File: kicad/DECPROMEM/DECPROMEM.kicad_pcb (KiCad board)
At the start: 2 copper layers, 127 x 134.6 mm, 114 parts, among them J10 BDAL08, J11 BDAL09, J12 BDAL10, J13 BDAL11, J14 BDAL12, J15 BDAL13, J16 BDAL14, J17 BDAL15, J18 BDAL16, J19 BDAL17, J2 BDAL00, J20 BDAL18, J21 BDAL19, J22 BDAL20, J23 BDAL21, J24 BRPLYL, J25 BMDENL, J26 BWRITEL, J27 BWLBL, J28 BWHBL, J29 BSDENL, J3 BDAL01, J30 SSnL, J31 BDSL, J32 BASL, J33 BIOSELL, J34 BDCOKH, J35 GND, J36 GND, J37 GND, J38 DAH00, J39 DAH01, J4 BDAL02, J40 DAH02, J41 DAH03, J42 DAH04, J43 DAH05, J44 DAH06, J45 DAH07, J46 DAH08, J47 DAH09, J48 DAH10, J49 DAH11, J5 BDAL03, J50 DAH12, J51 DAH13, J52 DAH14, J53 DAH15, J54 DAH16, J55 DAH17, J56 DAH18, J57 DAH19, J58 DAH20, J59 DAH21, J6 BDAL04, J60 JTAG, J61 ASL, J62 MDENL, J63 SDENL, J64 MOEL, J65 MWEL, J66 MCEHIGHL, J67 MCELOWH, J68 MLEL, J69 MHEL, J7 BDAL05, J70 BUSDIR, J71 BUSOE, J72 CLK, J73 MA15, J74 MA16, J75 MA17, J76 MA18, J77 MA19, J78 MA20, J79 MA21, J8 BDAL06, J80 HOLDL, J81 CSL, J82 SCK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

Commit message: More layout done.
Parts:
- added J85: BINITL, CompLibFootprint:Testpoint, F.Cu at (386.1, 203.8)
- moved J37 112.5 mm to (391.8, 124.5), turned to 0 degrees
- moved R2 88.6 mm to (368.9, 118.1), turned to -90 degrees
- moved C4 60.5 mm to (388.0, 129.5), turned to 90 degrees
- moved J36 54.7 mm to (283.2, 151.1), turned to 0 degrees
- moved C9 36.2 mm to (273.7, 170.2)
- moved C10 31.5 mm to (286.4, 137.2), turned to -90 degrees
- moved J79 30.3 mm to (362.6, 119.4), turned to 0 degrees
- moved J60 24.2 mm to (278.1, 194.3)
- moved C3 22.7 mm to (275.6, 132.1)
- moved R3 20.4 mm to (271.8, 137.2)
- moved J72 19.8 mm to (272.4, 146.7), turned to 0 degrees
- moved C5 18.1 mm to (364.5, 128.2), turned to 90 degrees
- moved J82 15.9 mm to (270.5, 123.2), turned to 180 degrees
- moved J84 14.9 mm to (285.8, 125.7), turned to 0 degrees
- moved J80 14.0 mm to (272.4, 125.7), turned to 180 degrees
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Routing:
- net GND: track 0.00 -> 678.4 mm, vias 0 -> 13
- net +5V: track 0.00 -> 548.8 mm, vias 0 -> 13
- net /BDCOKH: track 0.00 -> 186.3 mm, vias 0 -> 2
- net /BINITL: track 0.00 -> 182.3 mm, vias 0 -> 2
- net /BRPLYL: track 18.2 -> 177.0 mm, vias 0 -> 3
- net /MDENL: track 13.0 -> 158.2 mm, vias 0 -> 2
- net /BWHBL: track 18.1 -> 157.3 mm, vias 0 -> 2
- net /SSnL: track 18.2 -> 156.9 mm, vias 0 -> 2
- net /BMDENL: track 18.2 -> 156.2 mm, vias 0 -> 2
- net /BWRITEL: track 18.1 -> 152.2 mm, vias 0 -> 2
- net /BUSDIRH: track 14.9 -> 147.6 mm, vias 0 -> 2
- net /BUSOEL: track 7.26 -> 133.2 mm, vias 0 -> 4
- net /BSDENL: track 18.1 -> 140.6 mm, vias 0 -> 2
- net /BASL: track 17.1 -> 135.2 mm, vias 0 -> 4
- net /BIOSELL: track 18.1 -> 131.5 mm, vias 0 -> 2
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
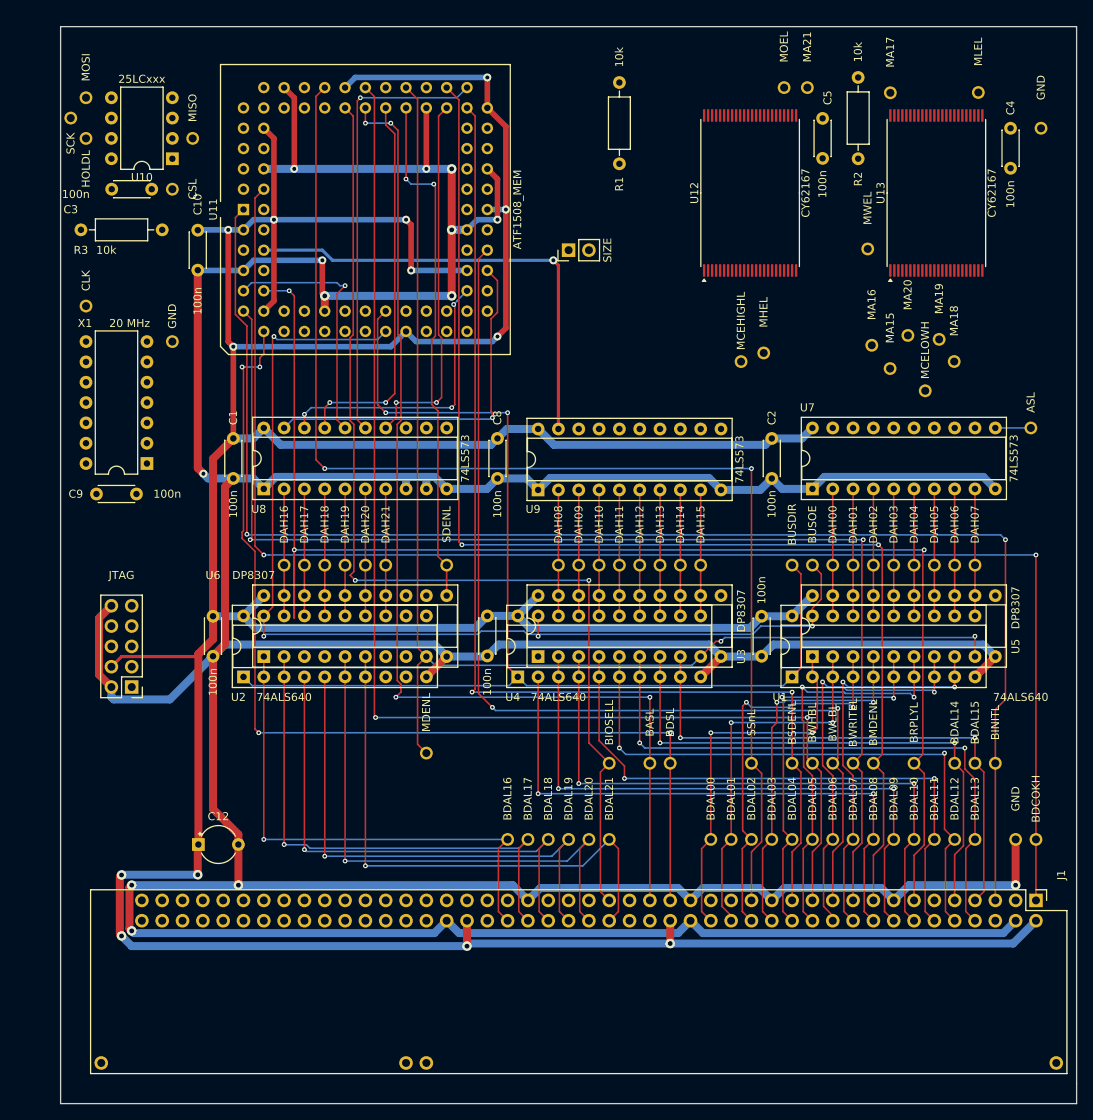
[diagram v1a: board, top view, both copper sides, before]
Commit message: Had to add more test points.
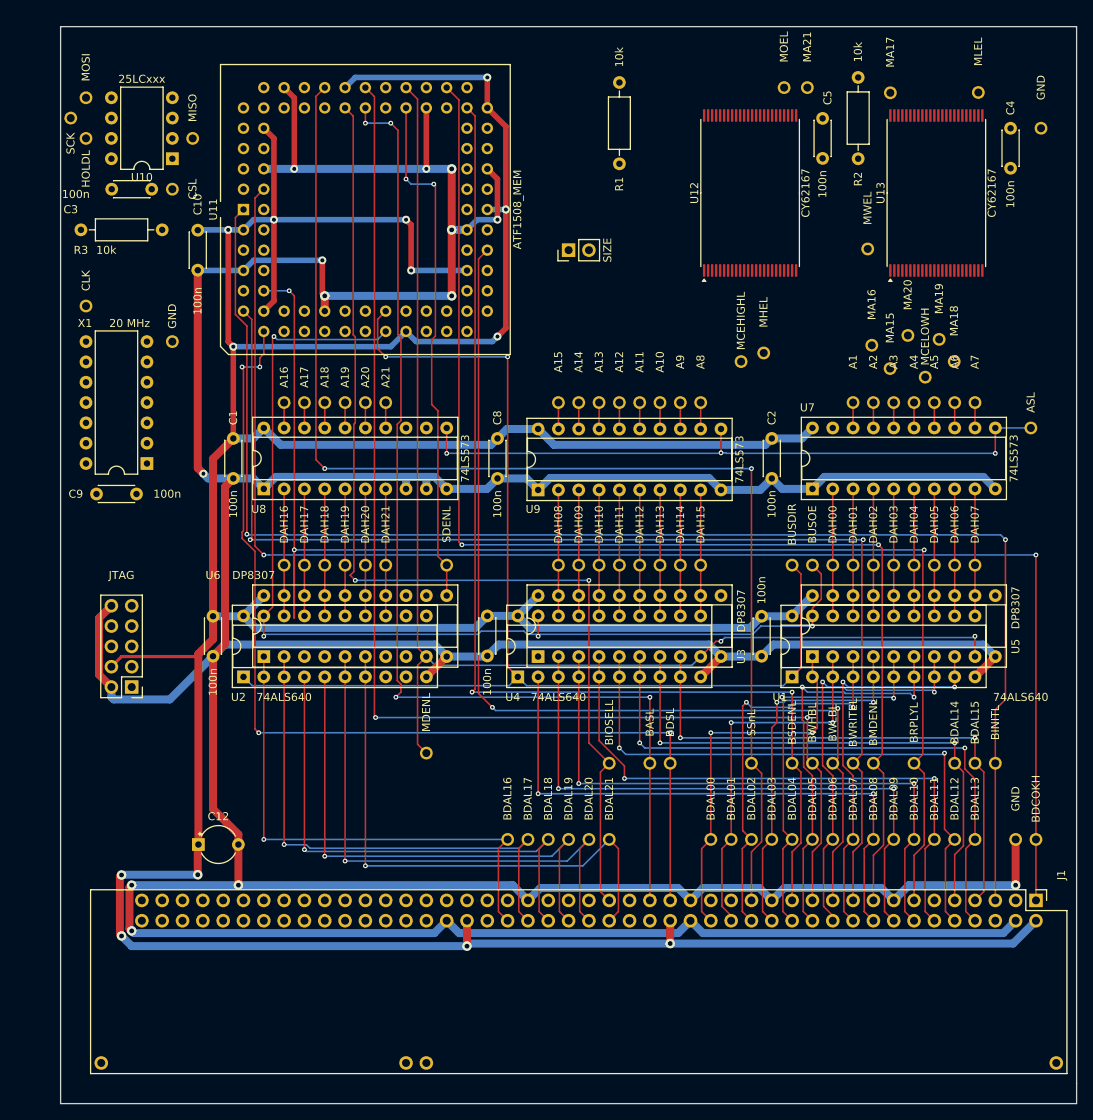
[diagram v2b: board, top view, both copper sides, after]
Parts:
- added J100: A15, CompLibFootprint:Testpoint, F.Cu at (331.5, 158.8)
- added J101: A16, CompLibFootprint:Testpoint, F.Cu at (297.2, 158.8)
- added J102: A17, CompLibFootprint:Testpoint, F.Cu at (299.7, 158.8)
- added J103: A18, CompLibFootprint:Testpoint, F.Cu at (302.3, 158.8)
- added J104: A19, CompLibFootprint:Testpoint, F.Cu at (304.8, 158.8)
- added J105: A20, CompLibFootprint:Testpoint, F.Cu at (307.3, 158.8)
- added J106: A21, CompLibFootprint:Testpoint, F.Cu at (309.9, 158.8)
- added J86: A1, CompLibFootprint:Testpoint, F.Cu at (368.3, 158.8)
- added J87: A2, CompLibFootprint:Testpoint, F.Cu at (370.8, 158.8)
- added J88: A3, CompLibFootprint:Testpoint, F.Cu at (373.4, 158.8)
- added J89: A4, CompLibFootprint:Testpoint, F.Cu at (375.9, 158.8)
- added J90: A5, CompLibFootprint:Testpoint, F.Cu at (378.5, 158.8)
- added J91: A6, CompLibFootprint:Testpoint, F.Cu at (381.0, 158.8)
- added J92: A7, CompLibFootprint:Testpoint, F.Cu at (383.5, 158.8)
- added J93: A8, CompLibFootprint:Testpoint, F.Cu at (349.2, 158.8)
- added J94: A9, CompLibFootprint:Testpoint, F.Cu at (346.7, 158.8)
- added J95: A10, CompLibFootprint:Testpoint, F.Cu at (344.2, 158.8)
- added J96: A11, CompLibFootprint:Testpoint, F.Cu at (341.6, 158.8)
- added J97: A12, CompLibFootprint:Testpoint, F.Cu at (339.1, 158.8)
- added J98: A13, CompLibFootprint:Testpoint, F.Cu at (336.6, 158.8)
- added J99: A14, CompLibFootprint:Testpoint, F.Cu at (334.0, 158.8)
- moved J67 1.71 mm to (377.3, 155.6)
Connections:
- U7 pad 12: unconnected-(U7-Q7-Pad12) -> /A7
- U7 pad 13: /A7 -> /A6
- U7 pad 14: /A6 -> /A5
- U7 pad 15: /A5 -> /A4
- U7 pad 16: /A4 -> /A3
- U7 pad 17: /A3 -> /A2
- U7 pad 18: /A2 -> /A1
- U7 pad 19: /A1 -> unconnected-(U7-Q0-Pad19)
- U8 pad 14: /A16 -> /A21
- U8 pad 15: /A17 -> /A20
- U8 pad 16: /A18 -> /A19
- U8 pad 17: /A19 -> /A18
- U8 pad 18: /A20 -> /A17
- U8 pad 19: /A21 -> /A16
- U9 pad 12: /A8 -> /A15
- U9 pad 13: /A9 -> /A14
- U9 pad 14: /A10 -> /A13
- U9 pad 15: /A11 -> /A12
- U9 pad 16: /A12 -> /A11
- U9 pad 17: /A13 -> /A10
- U9 pad 18: /A14 -> /A9
- U9 pad 19: /A15 -> /A8
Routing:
- net /ASL: track 4.44 -> 82.4 mm, vias 0 -> 3
- net /A15: track 58.1 -> 3.30 mm, vias 1 -> 0
- net /A17: track 55.7 -> 3.18 mm, vias 1 -> 0
- net /A19: track 48.2 -> 3.18 mm, vias 2 -> 0
- net /A16: track 46.4 -> 3.18 mm, vias 2 -> 0
- net /A21: track 45.9 -> 3.18 mm, vias 1 -> 0
- net /A20: track 36.0 -> 3.18 mm, vias 3 -> 0
- net /A18: track 31.9 -> 3.18 mm, vias 1 -> 0
- net /A9: track 0.00 -> 3.30 mm
- net /A8: track 0.00 -> 3.30 mm
- net /A14: track 0.00 -> 3.30 mm
- net /A13: track 0.00 -> 3.30 mm
- net /A12: track 0.00 -> 3.30 mm
- net /A11: track 0.00 -> 3.30 mm
- net /A10: track 0.00 -> 3.30 mm
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
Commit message: Added pdf file and all the gerbers
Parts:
- moved J61 63.3 mm to (327.4, 157.5)
- moved J76 46.4 mm to (334.6, 149.9), turned to -90 degrees
- moved J73 45.7 mm to (334.6, 129.5), turned to -90 degrees
- moved J67 43.5 mm to (335.8, 142.6), turned to -90 degrees
- moved J74 35.7 mm to (335.2, 147.2)
- moved R2 25.6 mm to (391.8, 129.5)
- moved J78 21.8 mm to (353.6, 147.2), turned to -90 degrees
- moved J77 21.0 mm to (358.1, 153.0), turned to 180 degrees
- moved J68 20.4 mm to (367.2, 131.6)
- moved JP1 17.9 mm to (334.8, 121.9), turned to 180 degrees
- moved J93 17.7 mm to (331.6, 158.8)
- moved J100 17.7 mm to (349.1, 158.8)
- moved J79 16.6 mm to (367.2, 135.3)
- moved J80 14.3 mm to (286.7, 125.2)
- moved C5 13.5 mm to (355.3, 118.4), turned to 180 degrees
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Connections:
- J100 pad 1: /A8 -> /A15
- J93 pad 1: /A15 -> /A8
- J94 pad 1: /A14 -> /A9
- J95 pad 1: /A13 -> /A10
- J96 pad 1: /A12 -> /A11
- J97 pad 1: /A11 -> /A12
- J98 pad 1: /A10 -> /A13
- J99 pad 1: /A9 -> /A14
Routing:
- net GND: track 678.4 -> 886.1 mm, vias 13 -> 23
- net /DAH0: track 15.9 -> 197.9 mm, vias 0 -> 7
- net /DAH1: track 15.9 -> 197.0 mm, vias 0 -> 7
- net +5V: track 548.8 -> 716.5 mm, vias 13 -> 18
- net /DAH2: track 15.9 -> 183.5 mm, vias 0 -> 6
- net /DAH6: track 15.9 -> 179.4 mm, vias 0 -> 8
- net /DAH7: track 15.9 -> 170.2 mm, vias 0 -> 4
- net /DAH4: track 15.9 -> 168.7 mm, vias 0 -> 6
- net /DAH5: track 15.9 -> 166.7 mm, vias 0 -> 7
- net /DAH3: track 15.9 -> 166.7 mm, vias 0 -> 4
- net /A2: track 3.18 -> 135.7 mm, vias 0 -> 7
- net /A1: track 3.18 -> 132.0 mm, vias 0 -> 4
- net /MOEL: track 0.00 -> 125.2 mm, vias 0 -> 3
- net /A3: track 3.18 -> 117.4 mm, vias 0 -> 6
- net /DAH9: track 15.7 -> 124.6 mm, vias 0 -> 3
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- added copper zone on B.Cu, net +5V
- added copper zone on F.Cu, net GND
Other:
- board text added: "1"
- board text added: "2 or 4 meg memory board for DEC Professional"
- board text added: "Mattis Lind 2025"
- board text added: "https://github.com/MattisLind/DECPROMEM"
- board text added: "www.datormuseum.se"

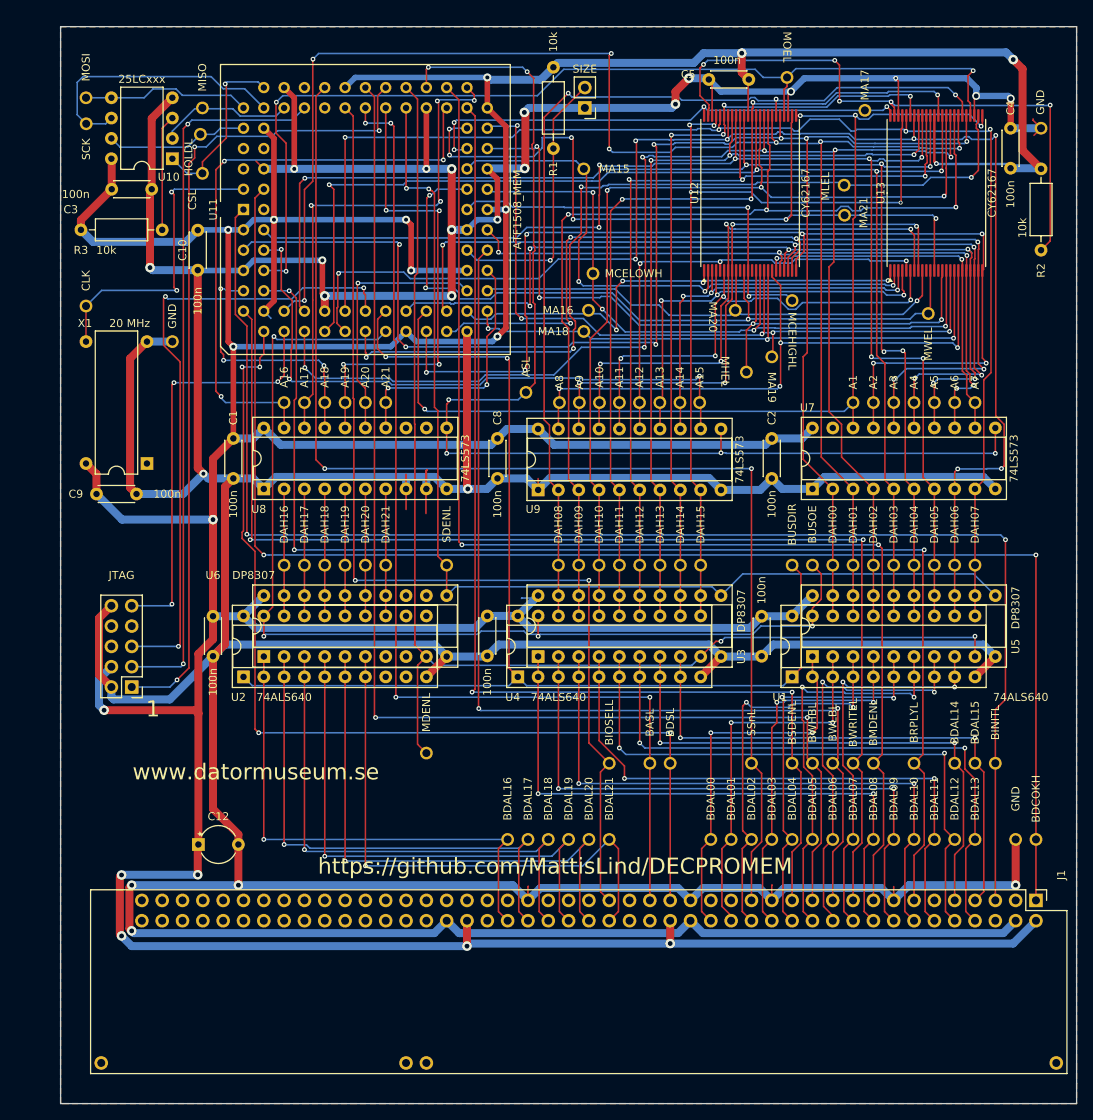
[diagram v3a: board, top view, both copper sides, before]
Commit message: Updated the schematics and layout to fix a bunch small errors.
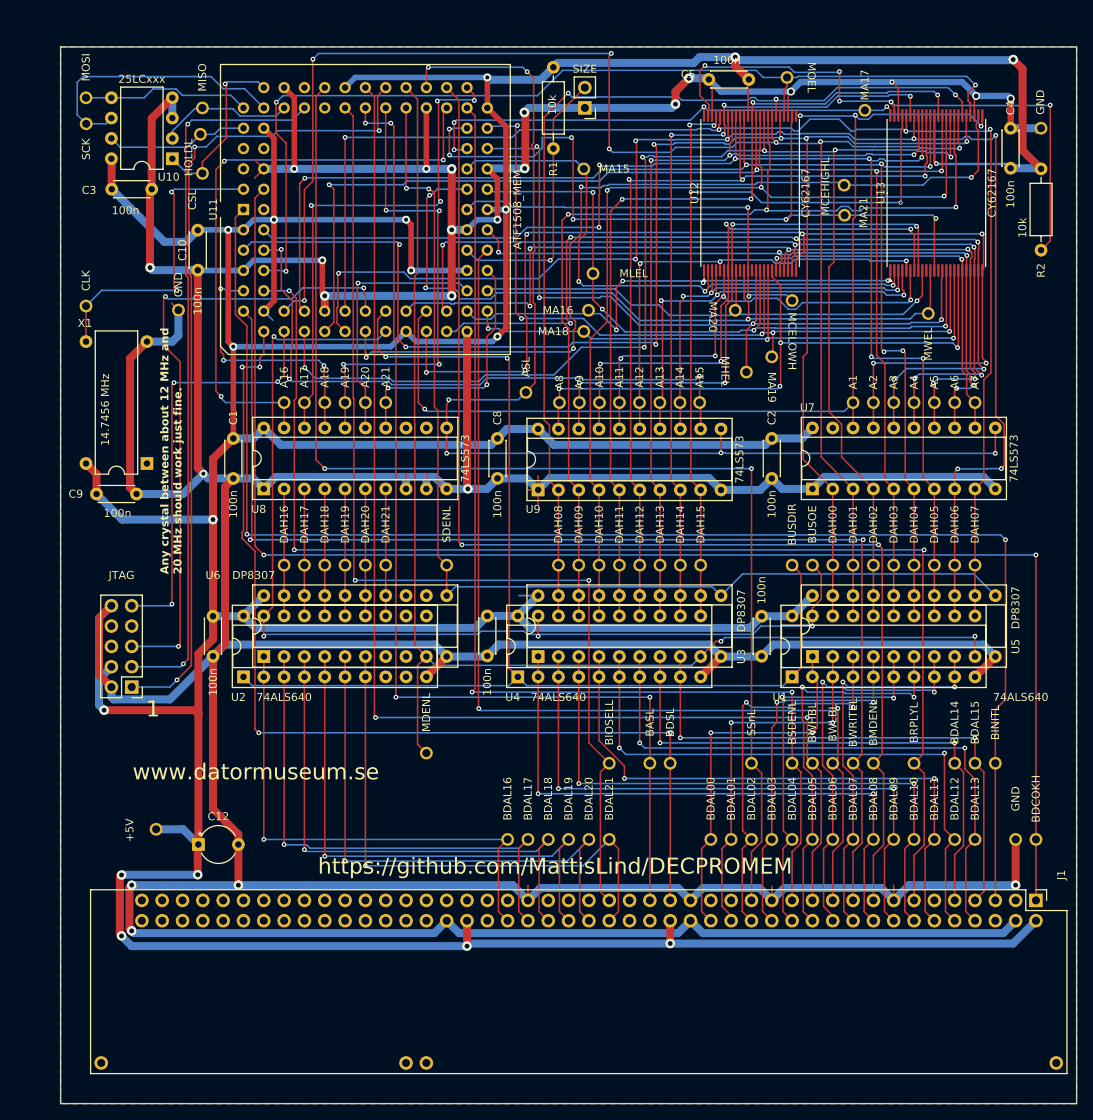
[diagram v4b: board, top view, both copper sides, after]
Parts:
- removed R3: 10k, Resistor_THT:R_Axial_DIN0207_L6.3mm_D2.5mm_P10.16mm_Horizontal
- added J107: +5V, CompLibFootprint:Testpoint, F.Cu at (281.2, 212.1)
- J66: value MCEHIGHL -> MCELOWH
- J67: value MCELOWH -> MLEL
- J68: value MLEL -> MCEHIGHL
- X1: value 20 MHz -> 14.7456 MHz
- moved J36 4.01 mm to (284.0, 147.2)
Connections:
- J66 pad 1: /MCEHIGHL -> /MCELOWH
- J67 pad 1: /MCELOWH -> /MLEL
- J68 pad 1: /MLEL -> /MCEHIGHL
- U10 pad 3: Net-(U10-~{WP}) -> GND
- U11 pad 22: /MLEL -> /MCEHIGHL
- U11 pad 44: /MCEHIGHL -> /MCELOWH
- U11 pad 45: /MCELOWH -> /MLEL
- U12 pad 12: /MCEHIGHL -> /MCELOWH
- U12 pad 15: /MCELOWH -> /MLEL
- U13 pad 15: /MCELOWH -> /MLEL
- U13 pad 26: /MLEL -> /MCEHIGHL
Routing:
- net /MCEHIGHL: track 53.8 -> 108.8 mm, vias 2 -> 4
- net /MCELOWH: track 87.7 -> 53.8 mm, vias 4 -> 2
- net /MLEL: track 108.8 -> 87.7 mm
- net GND: track 886.1 -> 866.3 mm
- net Net-(U10-~{WP}): track 14.5 -> 0.00 mm
- net +5V: track 716.5 -> 710.5 mm
- net /MOEL: track 125.2 -> 123.6 mm
- net /PULLUP: track 76.1 -> 75.0 mm
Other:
- board size 127 x 134.6 mm -> 127 x 132.1 mm
- board text added: "2 or 4 meg memory board for DEC Professional (spin 2)"
- board text added: "Any crystal between about 12 MHz and 20 MHz should work just fine."
- board text removed: "2 or 4 meg memory board for DEC Professional"

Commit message: Updating pinout for large connector since it was wrong. Added support for 245 trancerivers.
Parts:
- added JP2: NONINVERTING, Connector_PinHeader_2.54mm:PinHeader_1x02_P2.54mm_Vertical, F.Cu at (276.5, 140.6)
- added R3: 10k, Resistor_THT:R_Axial_DIN0207_L6.3mm_D2.5mm_P10.16mm_Horizontal, F.Cu at (272.2, 132.1)
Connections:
- U11 pad 2: (no net) -> Net-(JP2-B)
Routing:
- net Net-(JP2-B): track 0.00 -> 27.3 mm, vias 0 -> 1
- net +5V: track 710.5 -> 723.7 mm
- net GND: track 866.3 -> 879.4 mm
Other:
- board text added: "The NONINVERTING jumper shall be installed if 245 type tranceivers are being used."
